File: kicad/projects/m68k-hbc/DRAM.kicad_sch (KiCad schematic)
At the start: 32 parts, among them J1 JTAG_DRAMC, U10 74LS245, U11 MCP23017_SO, U21 SIMM72 Slot A, U22 SIMM72 Slot B, U23 SIMM72 Slot C, U24 SIMM72 Slot D, U4 EPM7128SLC84 / DRAM Controller, U6 74LS137, U7 74LS245, U8 74LS245, U9 74LS245, X5 70M

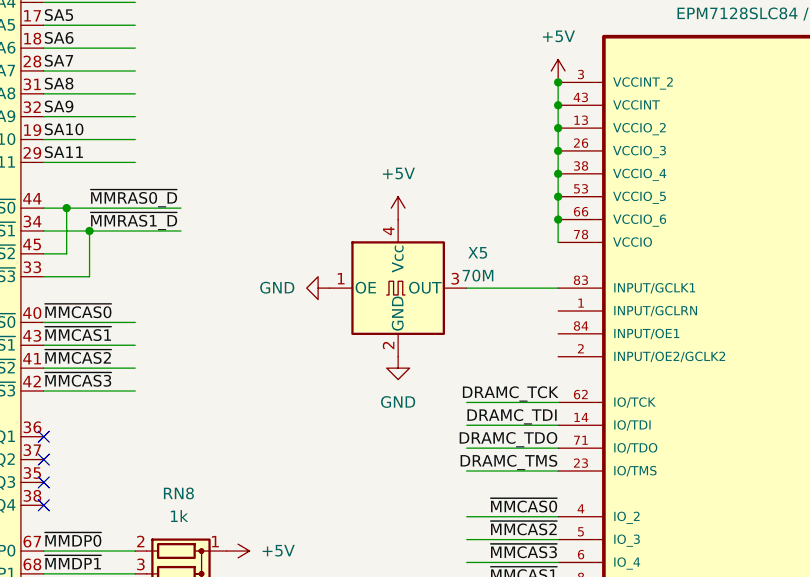
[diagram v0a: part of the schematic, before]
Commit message: Modified system architecture, New KiCad Project: Cache Memory Module(SIMM80)
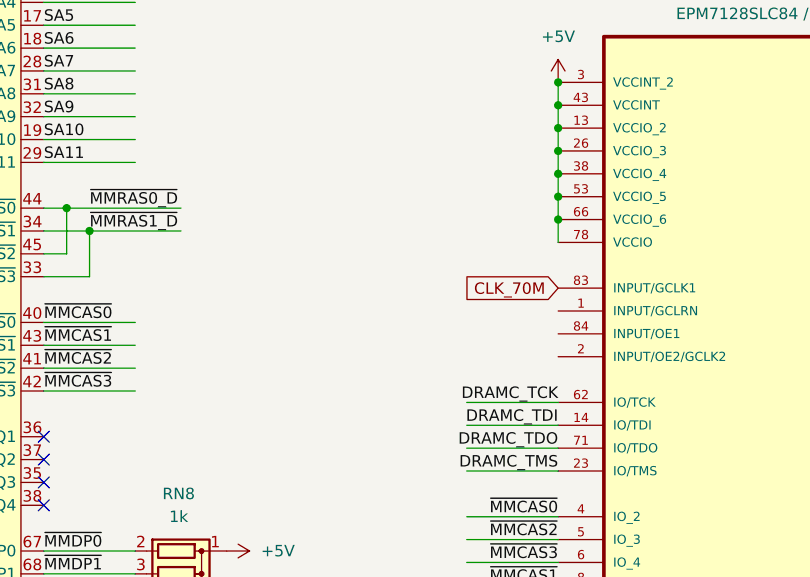
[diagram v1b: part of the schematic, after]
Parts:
- removed X5: 70M, Oscillator:Oscillator_SMD_SeikoEpson_SG8002CA-4Pin_7.0x5.0mm, symbol Oscillator:SG-8002CA
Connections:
- net CLK_70M: now reaches U4.83 (INPUT/GCLK1)
